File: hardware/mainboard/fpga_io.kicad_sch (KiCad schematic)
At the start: 24 parts, among them U1 LIFCL_40_CABGA400, X1 XO32

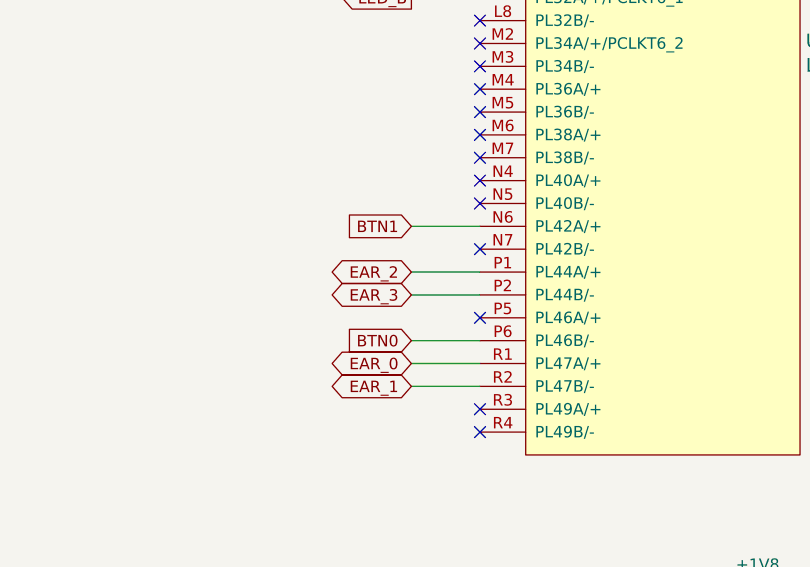
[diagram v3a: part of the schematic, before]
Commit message: Use 3-pin connector for ears
Signed-off-by: gatecat <gatecat@ds0.me>
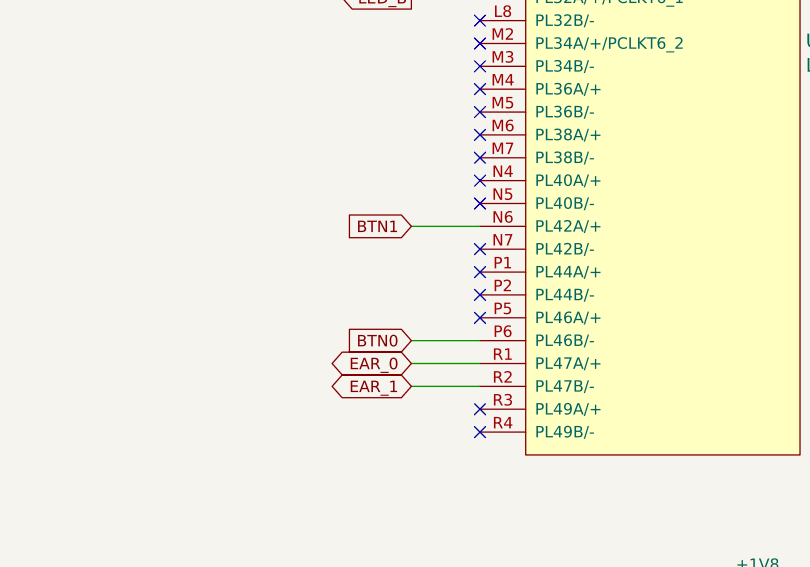
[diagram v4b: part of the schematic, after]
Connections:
- net EAR_2: no longer names the net of U1.P1 (PL44A/+)
- net EAR_3: no longer names the net of U1.P2 (PL44B/-)
- no-connect marks 73 -> 75
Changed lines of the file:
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@@
   (no_connect (at 331.47 88.9))
   (no_connect (at 331.47 93.98))
+  (no_connect (at 331.47 96.52))
+  (no_connect (at 331.47 99.06))
   (no_connect (at 331.47 101.6))
   (no_connect (at 331.47 111.76))
@@
     (stroke (width 0) (type solid) (color 0 0 0 0))
   )
-  (wire (pts (xy 323.85 96.52) (xy 331.47 96.52))
-    (stroke (width 0) (type solid) (color 0 0 0 0))
-  )
-  (wire (pts (xy 323.85 99.06) (xy 331.47 99.06))
-    (stroke (width 0) (type solid) (color 0 0 0 0))
-  )
   (wire (pts (xy 323.85 104.14) (xy 331.47 104.14))
     (stroke (width 0) (type solid) (color 0 0 0 0))
@@
       (effects (font (size 1.27 1.27)) (justify right) hide)
     )
-  )
-  (global_label "EAR_2" (shape bidirectional) (at 323.85 96.52 180)
-    (effects (font (size 1.27 1.27)) (justify right))
-    (property "Intersheet References" "${INTERSHEET_REFS}" (id 0) (at 314.2281 96.4406 0)
-      (effects (font (size 1.27 1.27)) (justify right) hide)
-    )
-  )
-  (global_label "EAR_3" (shape bidirectional) (at 323.85 99.06 180)
-    (effects (font (size 1.27 1.27)) (justify right))
-    (property "Intersheet References" "${INTERSHEET_REFS}" (id 0) (at 314.2281 98.9806 0)
-      (effects (font (size 1.27 1.27)) (justify right) hide)
-    )

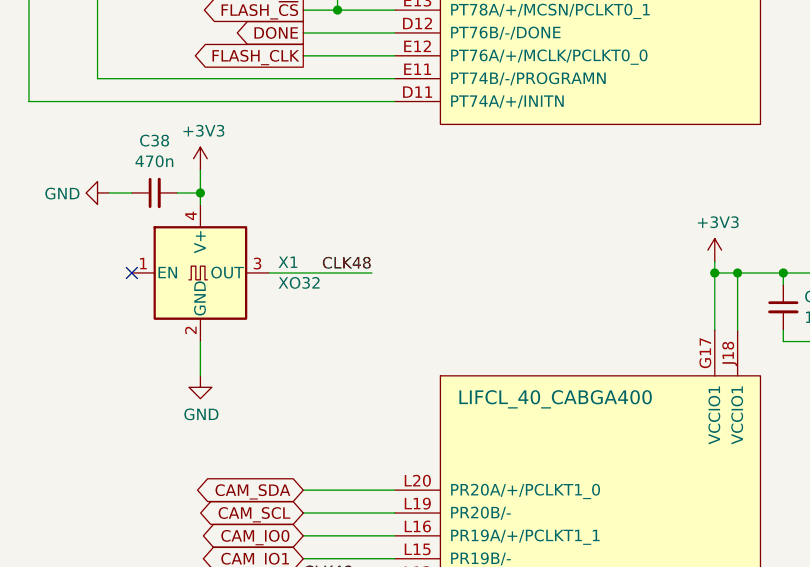
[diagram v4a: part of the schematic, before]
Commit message: Update some part numbers
Signed-off-by: gatecat <gatecat@ds0.me>
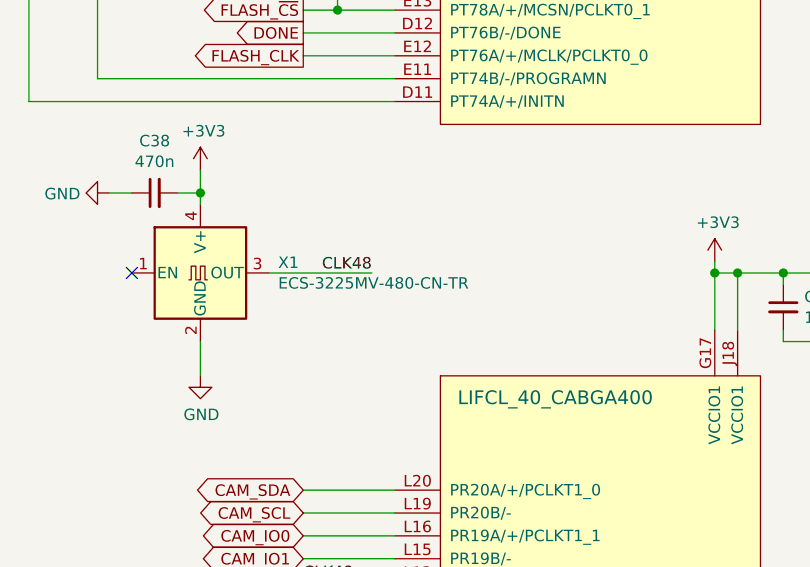
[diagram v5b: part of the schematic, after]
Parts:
- X1: value XO32 -> ECS-3225MV-480-CN-TR
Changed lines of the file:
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@@
       (effects (font (size 1.27 1.27)) (justify left))
     )
-    (property "Value" "XO32" (id 1) (at 48.0061 92.5893 0)
+    (property "Value" "ECS-3225MV-480-CN-TR" (id 1) (at 48.0061 92.5893 0)
       (effects (font (size 1.27 1.27)) (justify left))
     )
